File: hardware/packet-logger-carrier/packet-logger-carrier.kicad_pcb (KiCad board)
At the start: 2 copper layers, 86 x 58 mm, 22 parts, among them J1 RAK19003 J6, J10 RAK SPARE, J11 ESP SPARE, J12 BATT IN, J13 BATT JST-PH, J14 BATT TO RAK, J15 J15, J2 RAK19003 J7, J3 XIAO ESP32-C6, J4 microSD, J5 LID CABLE, SW1 USER BUTTON, SW2 POWER SWITCH

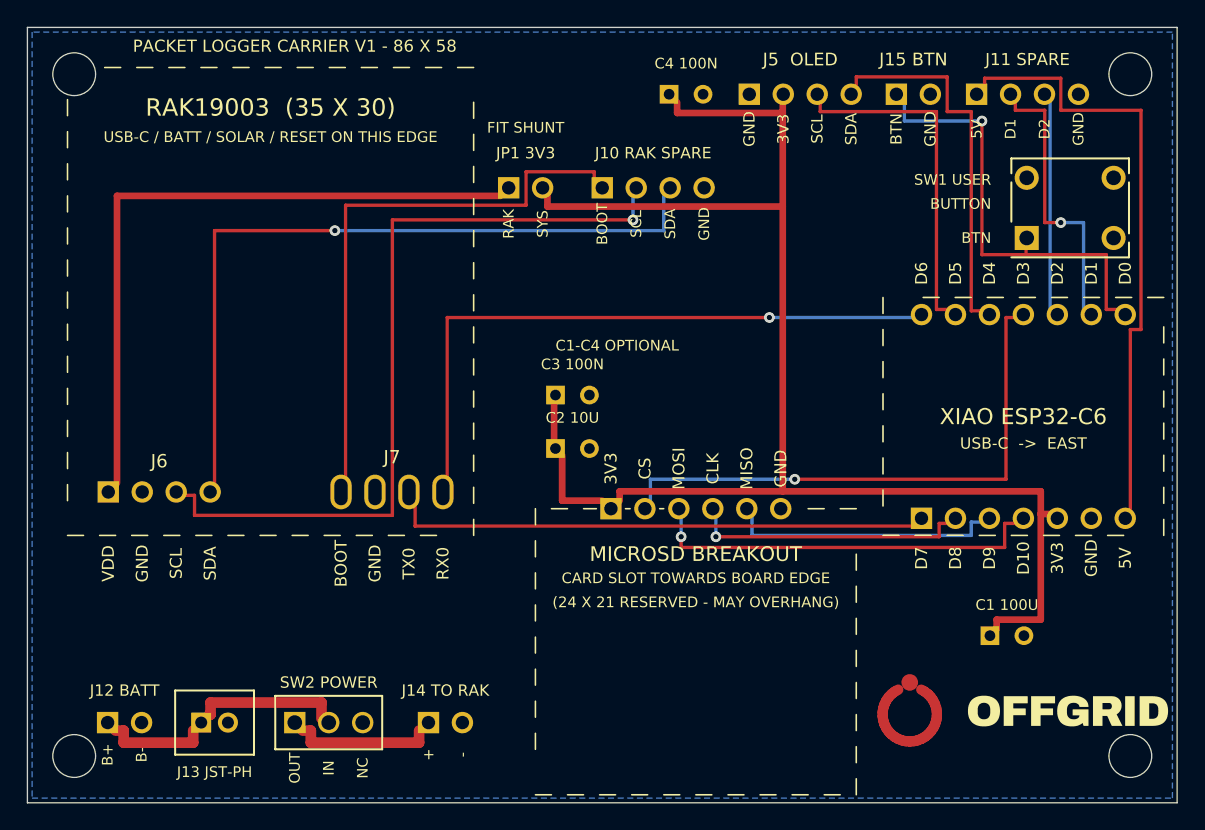
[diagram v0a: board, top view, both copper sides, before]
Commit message: hardware: route into pad centres, raise clearance to 0.30 mm
Reviewer said to add space between traces and pads, and to stop traces
coming out at an angle towards neighbouring pads. Measured both before
touching anything (src/style_audit.py):

  spacing     tightest 0.250 mm - exactly the design rule, 2x the 0.127 mm
              fab minimum. Not a manufacturing risk, but 38 spots sat on
              the floor with no margin.
  pad entry   51 of 51 terminations were off centre, worst 1.104 mm. The
              router treated ANY cell of a pad as arrival, so traces
              stopped wherever they first touched the copper - often the
              rim. That is the real defect: it leaves an acute trace/pad
              corner (an etch trap) and hangs the joint on the thinnest
              part of the annular ring.

Fixes:
  - router arrival is now the pad CENTRE (+-0.055 mm), not the whole pad.
    Oval slots still accept entry along their long axis, which is what an
    oval pad is for.
  - clearance 0.25 -> 0.30 mm. Swept 0.25/0.30/0.35: 0.30 routes with
    FEWER vias than 0.25 (8 vs 9) because the extra room lets traces take
    straighter paths. 0.35 pushed it back up to 10. 0.30 it is.
  - drc.py and the KiCad net class updated to match, so all three agree.

After:
  spacing     tightest 0.300 mm; nothing below it; 188 of 270 above 0.60
  pad entry   3 of 47 off centre, and all three are the J2 oval slots
              entered along their length. Everything else within 0.141 mm,
              which is the 0.1 mm routing grid quantisation.

Cost: 98 -> 102 track segments, vias unchanged at 8.

All gates pass. KiCad 10 DRC: 0 errors, 0 warnings, 0 unconnected.
Gerber round trip 0.0000 mm2 on both copper layers.

Co-Authored-By: Claude Opus 5 <noreply@anthropic.com>
Claude-Session: https://claude.ai/code/session_01RN9DXsTnQiAHDKajZRQGtQ
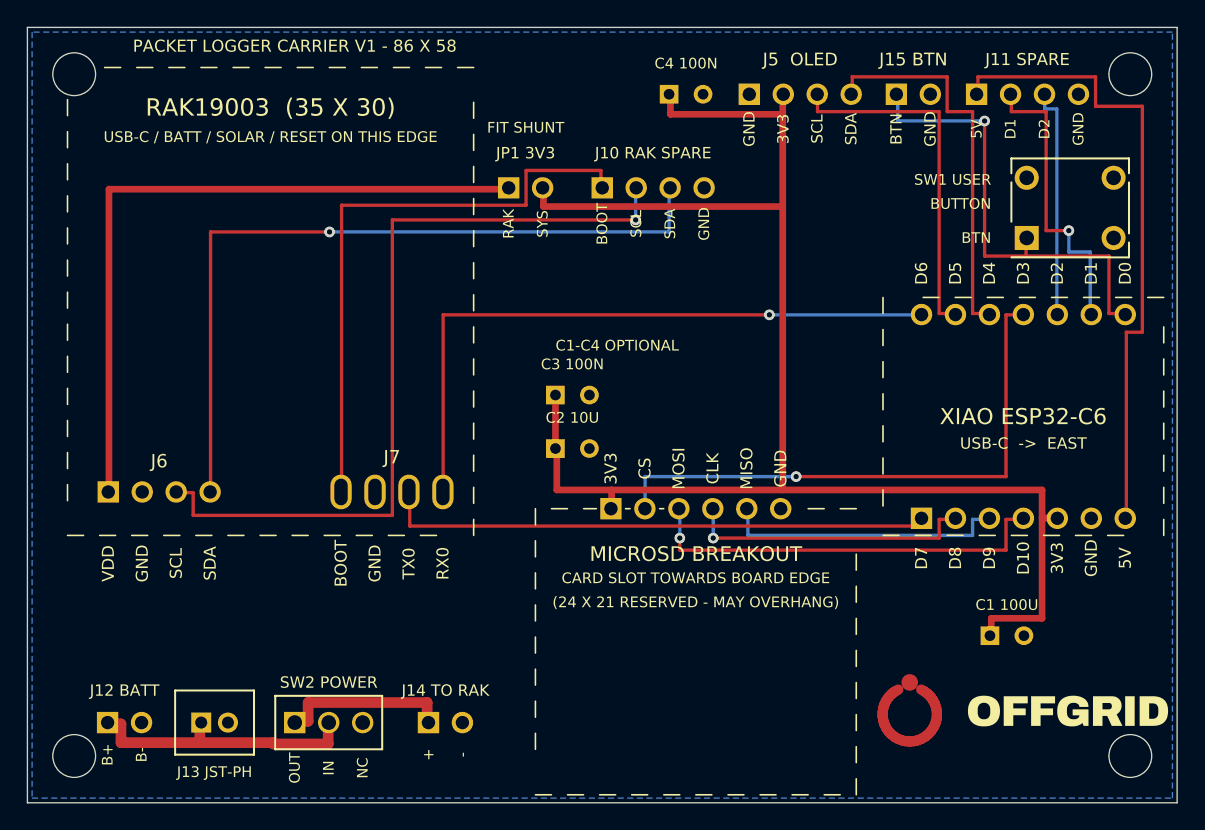
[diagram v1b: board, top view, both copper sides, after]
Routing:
- net +3V3: track 112.2 -> 118.6 mm
- net BAT+: track 18.1 -> 20.8 mm
- net BTN: track 32.0 -> 34.6 mm
- net XIAO_5V: track 45.5 -> 47.7 mm
- net RAW_3V3: track 50.2 -> 52.4 mm
- net BAT_SW: track 10.5 -> 12.6 mm
- net RAK_BOOT: track 42.1 -> 44.2 mm
- net RAK_TX0: track 38.8 -> 40.8 mm
- net SD_MOSI: track 29.2 -> 30.9 mm
- net SD_CLK: track 19.9 -> 21.6 mm
- net RAK_RX0: track 46.9 -> 48.5 mm
- net RAK_SDA: track 55.4 -> 56.9 mm
- net OLED_SCL: track 25.1 -> 26.6 mm
- net SD_CS: track 41.1 -> 42.6 mm
- net XIAO_D1: track 20.8 -> 22.2 mm
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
